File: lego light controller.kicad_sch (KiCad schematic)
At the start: 31 parts, among them J1 Conn_01x02, J2 Conn_01x02, J3 Conn_01x02, J4 Conn_01x03, J5 Conn_01x03, J7 Conn_01x06_Pin, P1 USB_C_Plug_USB2.0, Q1 BC847W, Q2 BC847W, Q3 BC847W, U1 ATSAMD11C14A-SS, U2 AMS1117-3.3

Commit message: add values and update usb c
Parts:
- removed R13, R14: R, Resistor_SMD:R_0402_1005Metric, symbol Device:R
- removed R3: R, Resistor_SMD:R_0603_1608Metric, symbol Device:R
- C1: value C_Polarized -> 10u
- C2: value C_Polarized -> 22u
- C3: value C -> 100n
- J1, J2, J3, J4, J5: now not fitted; now left out of the parts list
- P1: symbol Connector:USB_C_Plug_USB2.0 -> Connector:USB_C_Receptacle_USB2.0_14P
- R1, R12, R2: value R -> 5k1
- R10, R11: value R -> 470
- R4, R5, R6: value R -> 10k
- R7, R8, R9: value R -> 1k
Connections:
- net RUSB_N is gone; now on net USB_N: P1.A7 (D-)
- net RUSB_P is gone; now on net USB_P: P1.A6 (D+)
- net GND: now also R1.2, R2.2
- net USB_N: now also P1.B7 (D-)
- net USB_P: now also P1.B6 (D+)
- net at Q1.3 (C): now also J3.2 (Pin_2); no longer R1.1
- net at J1.2 (Pin_2): now also Q3.3 (C)
- net at R2.1: now also P1.B5 (CC2); no longer Q2.3 (C)
- net at P1.A5 (CC1): now also R1.1
- net at J2.2 (Pin_2): now also Q2.3 (C); no longer R2.2
- no-connect marks 0 -> 3

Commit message: update footprints and redo layout
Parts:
- P1: footprint Connector_USB:USB_C_Receptacle_JAE_DX07S016JA1R1500 -> Connector_USB:USB_C_Receptacle_GCT_USB4110
- Q1, Q2, Q3: footprint Package_TO_SOT_SMD:SOT-323_SC-70 -> Package_TO_SOT_SMD:SOT-23
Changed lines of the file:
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@@
       (effects (font (size 1.27 1.27)) (justify left))
     )
-    (property "Footprint" "Package_TO_SOT_SMD:SOT-323_SC-70" (at 247.65 62.865 0)
+    (property "Footprint" "Package_TO_SOT_SMD:SOT-23" (at 247.65 62.865 0)
       (effects (font (size 1.27 1.27) italic) (justify left) hide)
     )
@@
       (effects (font (size 1.27 1.27)) (justify left))
     )
-    (property "Footprint" "Package_TO_SOT_SMD:SOT-323_SC-70" (at 238.76 55.245 0)
+    (property "Footprint" "Package_TO_SOT_SMD:SOT-23" (at 238.76 55.245 0)
       (effects (font (size 1.27 1.27) italic) (justify left) hide)
     )
@@
       (effects (font (size 1.27 1.27)))
     )
-    (property "Footprint" "Connector_USB:USB_C_Receptacle_JAE_DX07S016JA1R1500" (at 76.2 167.64 0)
+    (property "Footprint" "Connector_USB:USB_C_Receptacle_GCT_USB4110" (at 76.2 167.64 0)
       (effects (font (size 1.27 1.27)) hide)
     )
@@
       (effects (font (size 1.27 1.27)) (justify left))
     )
-    (property "Footprint" "Package_TO_SOT_SMD:SOT-323_SC-70" (at 229.87 47.625 0)
+    (property "Footprint" "Package_TO_SOT_SMD:SOT-23" (at 229.87 47.625 0)
       (effects (font (size 1.27 1.27) italic) (justify left) hide)
     )

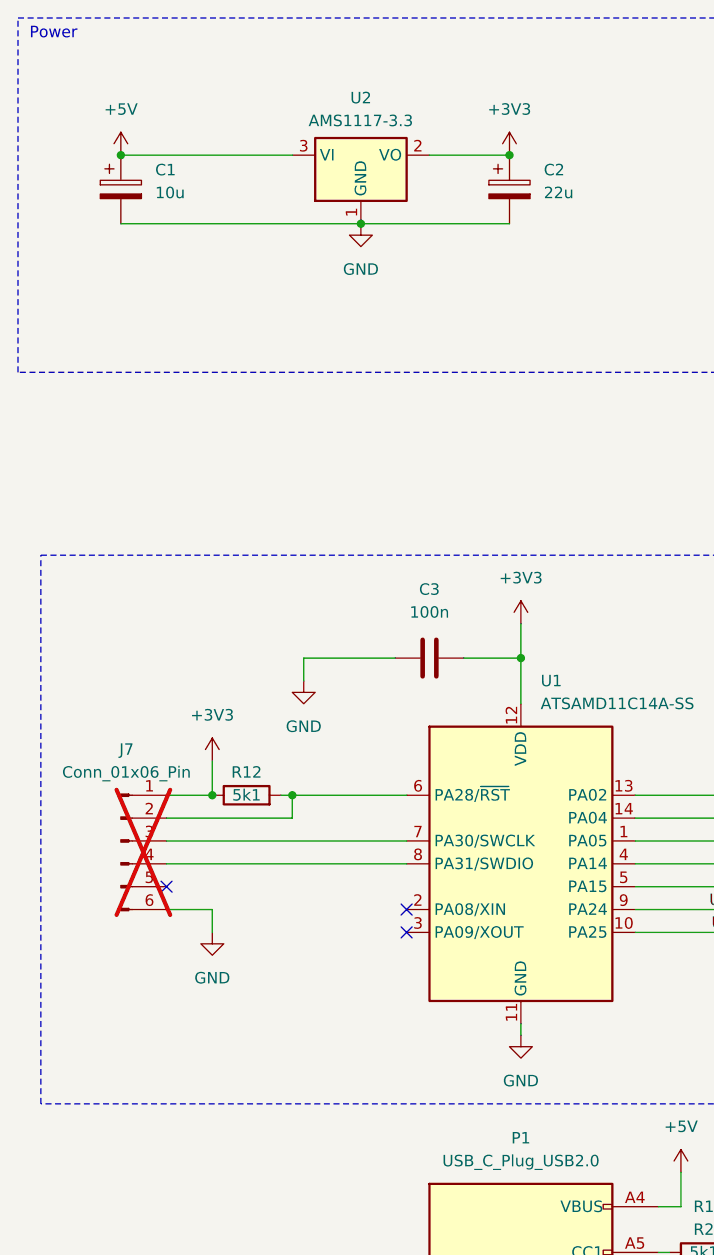
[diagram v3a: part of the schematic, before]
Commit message: add pads to unused io
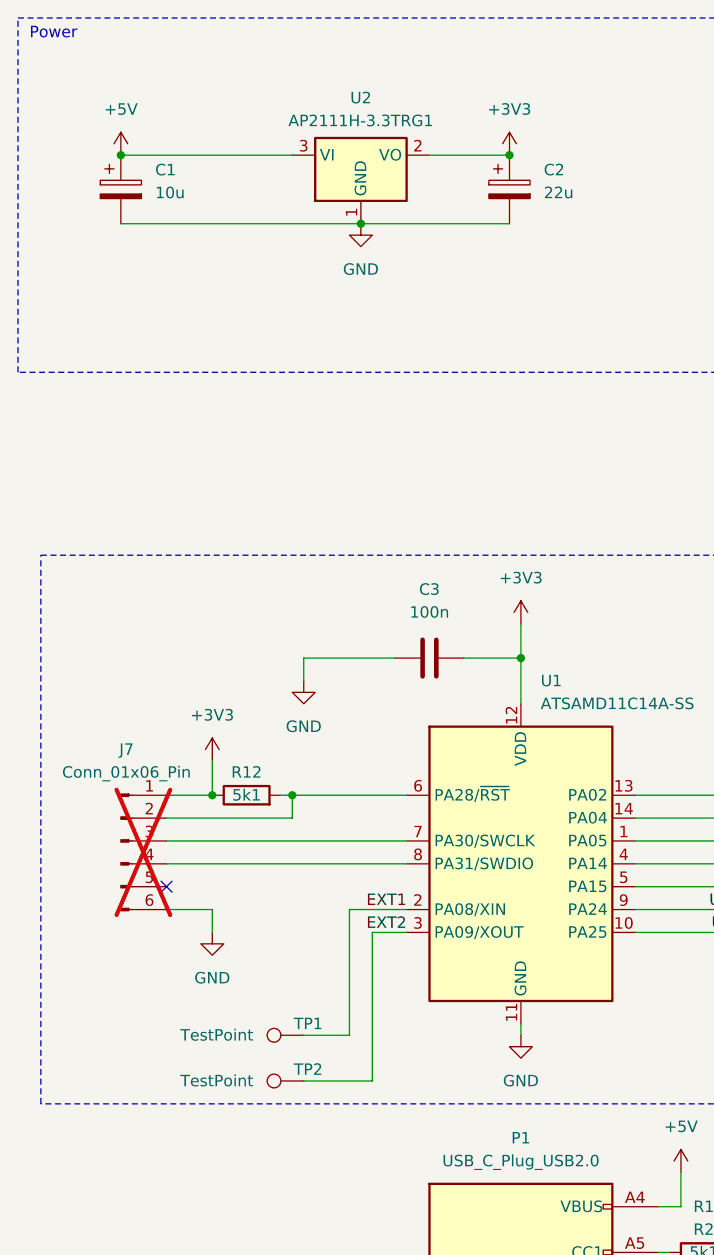
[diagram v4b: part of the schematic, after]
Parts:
- added TP1, TP2: TestPoint, TestPoint:TestPoint_Pad_2.0x2.0mm, symbol Connector:TestPoint
- U2: value AMS1117-3.3 -> AP2111H-3.3TRG1; MPN AMS1117-3.3 -> AP2111H-3.3TRG1
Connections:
- net EXT1: now reaches U1.2 (PA08/XIN)
- net EXT1: now also TP1.1
- net EXT2: now reaches U1.3 (PA09/XOUT)
- net EXT2: now also TP2.1
- no-connect marks 3 -> 1
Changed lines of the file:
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@@
   (junction (at 54.61 43.18) (diameter 0) (color 0 0 0 0)
   )
-  (no_connect (at 59.69 119.38))
   (no_connect (at 33.02 116.84))
-  (no_connect (at 59.69 121.92))
   (wire (pts (xy 250.19 109.22) (xy 257.81 109.22))
     (stroke (width 0) (type default))
@@
     (stroke (width 0) (type default))
   )
+  (wire (pts (xy 55.88 121.92) (xy 59.69 121.92))
+    (stroke (width 0) (type default))
+  )
   (wire (pts (xy 252.73 114.3) (xy 252.73 104.14))
     (stroke (width 0) (type default))
@@
     (stroke (width 0) (type default))
   )
+  (wire (pts (xy 48.26 138.43) (xy 55.88 138.43))
+    (stroke (width 0) (type default))
+  )
   (wire (pts (xy 250.19 99.06) (xy 257.81 99.06))
     (stroke (width 0) (type default))
@@
     (stroke (width 0) (type default))
   )
+  (wire (pts (xy 55.88 138.43) (xy 55.88 121.92))
+    (stroke (width 0) (type default))
+  )
   (wire (pts (xy 214.63 74.93) (xy 219.71 74.93))
     (stroke (width 0) (type default))
@@
     (stroke (width 0) (type default))
   )
+  (wire (pts (xy 59.69 119.38) (xy 53.34 119.38))
+    (stroke (width 0) (type default))
+  )
   (wire (pts (xy 68.58 190.5) (xy 68.58 191.77))
     (stroke (width 0) (type default))
@@
     (stroke (width 0) (type default))
   )
+  (wire (pts (xy 53.34 119.38) (xy 53.34 133.35))
+    (stroke (width 0) (type default))
+  )
   (wire (pts (xy 195.58 60.96) (xy 204.47 60.96))
     (stroke (width 0) (type default))
@@
   )
   (wire (pts (xy 46.99 106.68) (xy 46.99 109.22))
+    (stroke (width 0) (type default))
+  )
+  (wire (pts (xy 53.34 133.35) (xy 48.26 133.35))
     (stroke (width 0) (type default))
   )
@@
     (effects (font (size 1.27 1.27)) (justify right bottom))
   )
+  (label "EXT2" (at 59.69 121.92 180) (fields_autoplaced)
+    (effects (font (size 1.27 1.27)) (justify right bottom))
+  )
   (label "LED2" (at 99.06 109.22 180) (fields_autoplaced)
     (effects (font (size 1.27 1.27)) (justify right bottom))
@@
   )
   (label "USB_P" (at 96.52 170.18 180) (fields_autoplaced)
+    (effects (font (size 1.27 1.27)) (justify right bottom))
+  )
+  (label "EXT1" (at 59.69 119.38 180) (fields_autoplaced)
     (effects (font (size 1.27 1.27)) (justify right bottom))
   )
@@
       (effects (font (size 1.27 1.27)))
     )
-    (property "Value" "AMS1117-3.3" (at 54.61 31.75 0)
+    (property "Value" "AP2111H-3.3TRG1" (at 54.61 31.75 0)
       (effects (font (size 1.27 1.27)))
     )
@@
       (effects (font (size 1.27 1.27)) hide)
     )
-    (property "MPN" "AMS1117-3.3" (at 54.61 35.56 0)
+    (property "MPN" "AP2111H-3.3TRG1" (at 54.61 35.56 0)
       (effects (font (size 1.27 1.27)) hide)
     )
@@
     )
   )
+  (symbol (lib_id "Connector:TestPoint") (at 48.26 138.43 90) (unit 1)
+    (in_bom yes) (on_board yes) (dnp no)
+    (property "Reference" "TP2" (at 48.768 137.16 90)
+      (effects (font (size 1.27 1.27)))
+    )
+    (property "Value" "TestPoint" (at 38.608 138.43 90)
+      (effects (font (size 1.27 1.27)))
+    )
+    (property "Footprint" "TestPoint:TestPoint_Pad_2.0x2.0mm" (at 48.26 133.35 0)
+      (effects (font (size 1.27 1.27)) hide)
+    )
+    (property "Datasheet" "~" (at 48.26 133.35 0)
+      (effects (font (size 1.27 1.27)) hide)
+    )
+    (pin "1")
+    (instances
+      (project "lego light controller"
+        (path "/98f222a8-3f8d-4678-9dc7-d0db8bfd24c1"
+          (reference "TP2") (unit 1)
+        )
+      )
+    )
+  )
   (symbol (lib_id "Device:R") (at 92.71 157.48 90) (unit 1)
     (in_bom yes) (on_board yes) (dnp no)
@@
         )
       )
+    )
+  )
+  (symbol (lib_id "Connector:TestPoint") (at 48.26 133.35 90) (unit 1)
+    (in_bom yes) (on_board yes) (dnp no)
+    (property "Reference" "TP1" (at 48.768 132.08 90)
+      (effects (font (size 1.27 1.27)))
+    )
+    (property "Value" "TestPoint" (at 38.608 133.35 90)
+      (effects (font (size 1.27 1.27)))
+    )
+    (property "Footprint" "TestPoint:TestPoint_Pad_2.0x2.0mm" (at 48.26 128.27 0)
+      (effects (font (size 1.27 1.27)) hide)
+    )
+    (property "Datasheet" "~" (at 48.26 128.27 0)
+      (effects (font (size 1.27 1.27)) hide)
+    )
+    (pin "1")
+    (instances
+      (project "lego light controller"
+        (path "/98f222a8-3f8d-4678-9dc7-d0db8bfd24c1"
+          (reference "TP1") (unit 1)
+        )
+      )
